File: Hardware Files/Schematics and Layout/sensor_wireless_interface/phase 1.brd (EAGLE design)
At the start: 100 x 80 mm, 5 parts, among them U1 RHD2216

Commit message: updated pin assignment for better routing
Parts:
- turned JP1 to 270 degrees
- turned JP2 to 0 degrees
- flipped JP3 to the top
- turned JP4 to 0 degrees
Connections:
- removed net N$12 (its old number): JP1.10, U1.12
- removed net N$2 (its old number): JP1.3, U1.2
- removed net N$56 (its old number): JP3.2, U1.36
- new net N$1: JP1.12, U1.12
- new net N$14: JP1.13, U1.13
- new net N$50: JP3.2, U1.30
- net N$10: now also JP1.8, U1.8; no longer JP1.6, U1.10
- net N$11: now also JP1.10, U1.10; no longer JP1.8, U1.11
- net N$13: now also JP1.11, U1.11; no longer JP1.12, U1.13
- net N$15: now also U1.56; no longer U1.43
- net N$16: now also U1.54; no longer U1.44
- net N$17: now also U1.52; no longer U1.45
- net N$19: now also U1.50; no longer U1.46
- net N$20: now also U1.48; no longer U1.47
- net N$21: now also U1.46; no longer U1.48
- net N$22: now also U1.44; no longer U1.49
- net N$23: now also JP2.2, U1.55; no longer JP2.14, U1.56
- net N$24: now also JP2.4, U1.53; no longer JP2.12, U1.55
- net N$25: now also JP2.6, U1.51; no longer JP2.10, U1.54
- net N$26: now also U1.49; no longer U1.53
- net N$27: now also JP2.10, U1.47; no longer JP2.6, U1.52
- net N$28: now also JP2.12, U1.45; no longer JP2.4, U1.51
- net N$29: now also JP2.14, U1.43; no longer JP2.2, U1.50
- net N$3: now also JP1.2, U1.2; no longer JP1.5, U1.3
- net N$30: now also JP4.2; no longer JP4.3
- net N$31: now also JP4.3; no longer JP4.5
- net N$32: now also JP4.4; no longer JP4.7
- net N$33: now also JP4.5; no longer JP4.9
- net N$34: now also JP4.6; no longer JP4.11
- net N$35: now also JP4.7; no longer JP4.13
- net N$36: now also JP4.8; no longer JP4.14
- net N$37: now also JP4.9; no longer JP4.12
- net N$39: now also JP4.11; no longer JP4.8
- net N$4: now also JP1.3, U1.3; no longer JP1.7, U1.4
- net N$40: now also JP4.12; no longer JP4.6
- net N$41: now also JP4.13; no longer JP4.4
- net N$42: now also JP4.14; no longer JP4.2
- net N$44: now also U1.31; no longer U1.30
- net N$45: now also U1.33; no longer U1.31
- net N$46: now also U1.35; no longer U1.32
- net N$47: now also U1.37; no longer U1.33
- net N$48: now also U1.39; no longer U1.34
- net N$49: now also U1.41; no longer U1.35
- net N$5: now also JP1.5; no longer JP1.9
- net N$51: now also JP3.4, U1.32; no longer JP3.12, U1.41
- net N$52: now also JP3.6, U1.34; no longer JP3.10, U1.40
- net N$53: now also U1.36; no longer U1.39
- net N$54: now also JP3.10; no longer JP3.6
- net N$55: now also JP3.12, U1.40; no longer JP3.4, U1.37
- net N$6: now also JP1.7, U1.7; no longer JP1.11, U1.6
- net N$7: now also JP1.9, U1.9; no longer JP1.13, U1.7
- net N$8: now also JP1.4, U1.4; no longer JP1.2, U1.8
- net N$9: now also JP1.6, U1.6; no longer JP1.4, U1.9

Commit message: changed to more specific schematic
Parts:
- removed JP4: (no value), pinhead:2X07
- added C1: 100nF, capacitor-wima:C2.5-2
- added C2: 10nF, capacitor-wima:C2.5-2
- JP1: device pinhead:2X07 -> pinhead:1X02
- JP2: device pinhead:2X07 -> pinhead:2X16
- JP3: device pinhead:2X07 -> pinhead:1X04
- moved JP3 32.4 mm to (52.1, 17.8), turned to 0 degrees
- moved JP1 7.73 mm to (29.2, 47.0)
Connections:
- removed net N$11: JP1.10, U1.10
- removed net N$12: JP1.14, U1.14
- removed net N$13: JP1.11, U1.11
- removed net N$14: JP1.13, U1.13
- removed net N$15: JP2.1, U1.56
- removed net N$16: JP2.3, U1.54
- removed net N$17: JP2.5, U1.52
- removed net N$18: JP4.1, U1.15
- removed net N$19: JP2.7, U1.50
- removed net N$2: JP1.1, U1.1
- removed net N$20: JP2.9, U1.48
- removed net N$21: JP2.11, U1.46
- removed net N$22: JP2.13, U1.44
- removed net N$23: JP2.2, U1.55
- removed net N$24: JP2.4, U1.53
- removed net N$25: JP2.6, U1.51
- removed net N$26: JP2.8, U1.49
- removed net N$27: JP2.10, U1.47
- removed net N$28: JP2.12, U1.45
- removed net N$29: JP2.14, U1.43
- removed net N$3: JP1.2, U1.2
- removed net N$30: JP4.2, U1.16
- removed net N$31: JP4.3, U1.17
- removed net N$32: JP4.4, U1.18
- removed net N$33: JP4.5, U1.19
- removed net N$34: JP4.6, U1.20
- removed net N$35: JP4.7, U1.21
- removed net N$36: JP4.8, U1.22
- removed net N$37: JP4.9, U1.23
- removed net N$38: JP4.10, U1.24
- removed net N$39: JP4.11, U1.25
- removed net N$4: JP1.3, U1.3
- removed net N$40: JP4.12, U1.26
- removed net N$41: JP4.13, U1.27
- removed net N$42: JP4.14, U1.28
- removed net N$43: JP3.1, U1.29
- removed net N$44: JP3.3, U1.31
- removed net N$45: JP3.5, U1.33
- removed net N$46: JP3.7, U1.35
- removed net N$47: JP3.9, U1.37
- removed net N$48: JP3.11, U1.39
- removed net N$49: JP3.13, U1.41
- removed net N$5: JP1.5, U1.5
- removed net N$50: JP3.2, U1.30
- removed net N$51: JP3.4, U1.32
- removed net N$52: JP3.6, U1.34
- removed net N$53: JP3.8, U1.36
- removed net N$54: JP3.10, U1.38
- removed net N$55: JP3.12, U1.40
- removed net N$56: JP3.14, U1.42
- removed net N$6: JP1.7, U1.7
- removed net N$7: JP1.9, U1.9
- removed net N$8: JP1.4, U1.4
- removed net N$9: JP1.6, U1.6
- new net AUXIN2: U1.15
- new net AUXIN3: U1.16
- new net AUX_OUT: U1.27
- new net CS_N: U1.18
- new net CS_P: JP3.1, U1.19
- new net GND: C1.2, C2.2, JP1.2, U1.11, U1.12, U1.17, U1.29, U1.30, U1.32
- new net IN0_N: JP2.2, U1.8
- new net IN0_P: JP2.1, U1.9
- new net IN10_N: JP2.22, U1.44
- new net IN10_P: JP2.21, U1.45
- new net IN11_N: JP2.24, U1.42
- new net IN11_P: JP2.23, U1.43
- new net IN12_N: JP2.26, U1.40
- new net IN12_P: JP2.25, U1.41
- new net IN13_N: JP2.28, U1.38
- new net IN13_P: JP2.27, U1.39
- new net IN14_N: JP2.30, U1.36
- new net IN14_P: JP2.29, U1.37
- new net IN15_N: JP2.32, U1.34
- new net IN15_P: JP2.31, U1.35
- new net IN1_N: JP2.4, U1.6
- new net IN1_P: JP2.3, U1.7
- new net IN2_N: JP2.6, U1.4
- new net IN2_P: JP2.5, U1.5
- new net IN3_N: JP2.8, U1.2
- new net IN3_P: JP2.7, U1.3
- new net IN4_N: JP2.10, U1.56
- new net IN4_P: JP2.9, U1.1
- new net IN5_N: JP2.12, U1.54
- new net IN5_P: JP2.11, U1.55
- new net IN6_N: JP2.14, U1.52
- new net IN6_P: JP2.13, U1.53
- new net IN7_N: JP2.16, U1.50
- new net IN7_P: JP2.15, U1.51
- new net IN8_N: JP2.18, U1.48
- new net IN8_P: JP2.17, U1.49
- new net IN9_N: JP2.20, U1.46
- new net IN9_P: JP2.19, U1.47
- new net MISO_N: U1.24
- new net MISO_P: JP3.4, U1.25
- new net MOSI_N: U1.22
- new net MOSI_P: JP3.3, U1.23
- new net SCLK_N: U1.20
- new net SCLK_P: JP3.2, U1.21
- new net VDD: C1.1, JP1.1, U1.13, U1.26, U1.31
- net N$1: now also C2.1, U1.28; no longer JP1.12, U1.12
- net N$10: now also U1.33; no longer JP1.8, U1.8

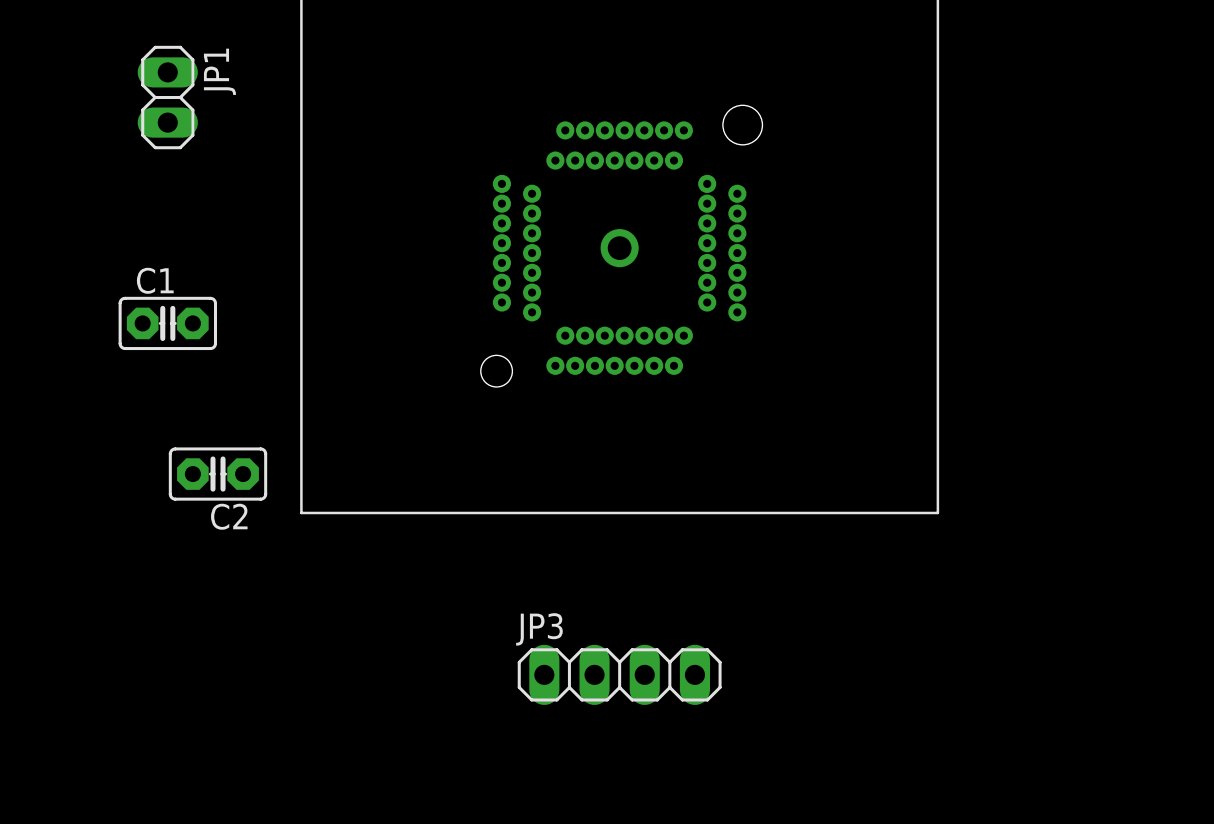
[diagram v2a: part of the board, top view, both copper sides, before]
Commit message: added another pin header for AUXIN*
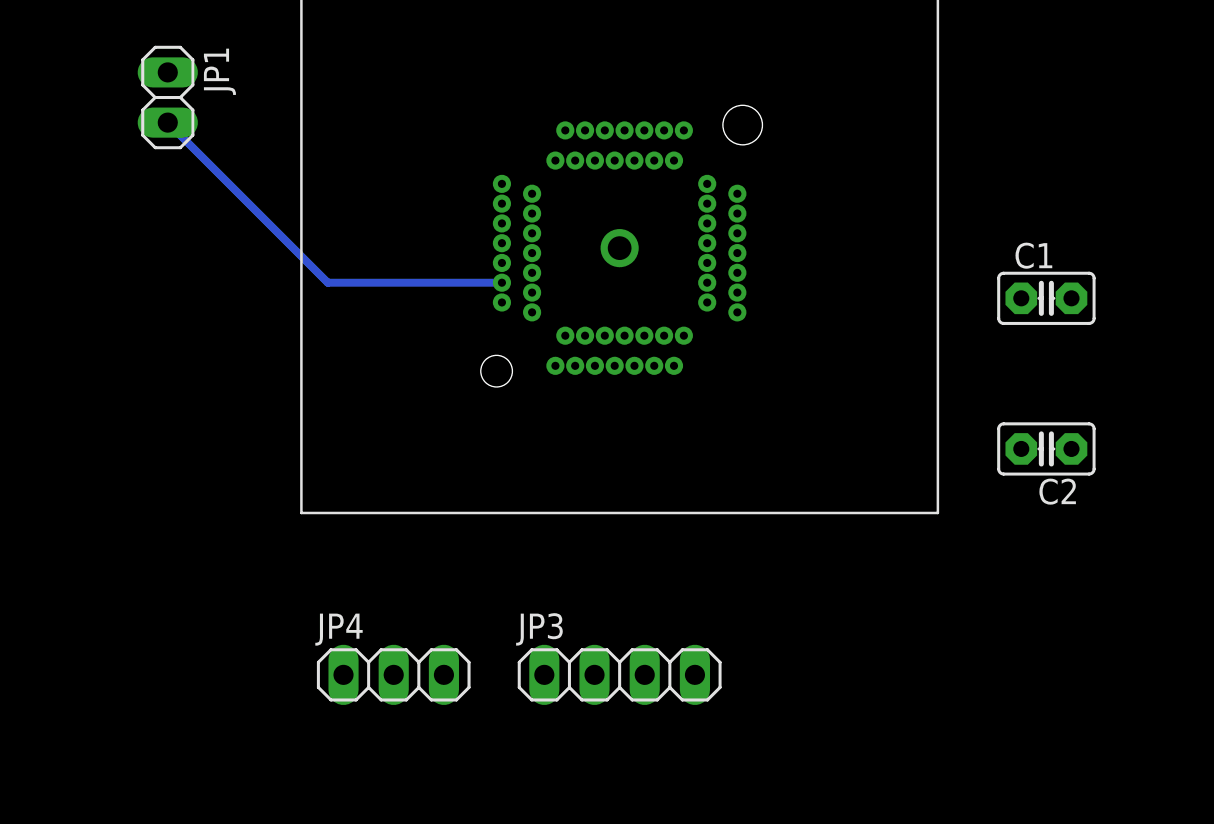
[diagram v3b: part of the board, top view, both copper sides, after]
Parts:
- added JP4: (no value), pinhead:1X03
- moved C1 44.5 mm to (73.7, 36.8)
- moved C2 41.9 mm to (73.7, 29.2)
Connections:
- removed net CS_N: U1.18
- removed net MISO_N: U1.24
- removed net MOSI_N: U1.22
- removed net N$10: U1.33
- removed net SCLK_N: U1.20
- new net AUXIN1: JP4.1, U1.14
- net AUXIN2: now also JP4.2
- net AUXIN3: now also JP4.3
- net GND: now also U1.10
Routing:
- net GND: track 0.00 -> 20.3 mm
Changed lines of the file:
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@@
 <element name="JP2" library="pinhead" package="2X16" value="" x="52.07" y="59.69"/>
 <element name="JP3" library="pinhead" package="1X04" value="" x="52.07" y="17.78"/>
-<element name="C1" library="capacitor-wima" package="C2.5-2" value="100nF" x="29.21" y="35.56"/>
-<element name="C2" library="capacitor-wima" package="C2.5-2" value="10nF" x="31.75" y="27.94" rot="R180"/>
+<element name="C1" library="capacitor-wima" package="C2.5-2" value="100nF" x="73.66" y="36.83"/>
+<element name="C2" library="capacitor-wima" package="C2.5-2" value="10nF" x="73.66" y="29.21" rot="R180"/>
+<element name="JP4" library="pinhead" package="1X03" value="" x="40.64" y="17.78"/>
 </elements>
 <signals>
@@
 <wire x1="46.115" y1="36.62" x2="54.32" y2="34.94" width="0" layer="19" extent="1-1"/>
 <wire x1="29.21" y1="48.26" x2="46.115" y2="36.62" width="0" layer="19" extent="1-1"/>
-<wire x1="27.94" y1="35.56" x2="29.21" y2="48.26" width="0" layer="19" extent="1-1"/>
+<wire x1="72.39" y1="36.83" x2="29.21" y2="48.26" width="0" layer="19" extent="1-1"/>
 </signal>
 <signal name="GND">
@@
 <contactref element="C2" pad="2"/>
 <contactref element="U1" pad="32"/>
+<contactref element="U1" pad="10"/>
+<wire x1="46.115" y1="37.62" x2="37.31" y2="37.62" width="0.4064" layer="16"/>
+<wire x1="37.31" y1="37.62" x2="29.21" y2="45.72" width="0.4064" layer="16"/>
 <wire x1="56.5" y1="37.62" x2="56.5" y2="36.62" width="0" layer="19" extent="1-1"/>
 <wire x1="58.025" y1="36.12" x2="56.5" y2="36.62" width="0" layer="19" extent="1-1"/>
 <wire x1="49.82" y1="33.415" x2="56.5" y2="36.62" width="0" layer="19" extent="1-1"/>
 <wire x1="47.64" y1="37.12" x2="49.82" y2="33.415" width="0" layer="19" extent="1-1"/>
+<wire x1="47.64" y1="38.12" x2="47.64" y2="37.12" width="0" layer="19" extent="1-1"/>
 <wire x1="46.115" y1="37.62" x2="47.64" y2="37.12" width="0" layer="19" extent="1-1"/>
-<wire x1="29.21" y1="45.72" x2="46.115" y2="37.62" width="0" layer="19" extent="1-1"/>
-<wire x1="30.48" y1="35.56" x2="29.21" y2="45.72" width="0" layer="19" extent="1-1"/>
-<wire x1="30.48" y1="27.94" x2="30.48" y2="35.56" width="0" layer="19" extent="1-1"/>
+<wire x1="74.93" y1="36.83" x2="37.31" y2="37.62" width="0" layer="19" extent="16-16"/>
+<wire x1="72.39" y1="29.21" x2="74.93" y2="36.83" width="0" layer="19" extent="1-1"/>
 </signal>
 <signal name="AUXIN2">
 <contactref element="U1" pad="15"/>
+<contactref element="JP4" pad="2"/>
+<wire x1="40.64" y1="17.78" x2="48.82" y2="33.415" width="0" layer="19" extent="1-1"/>
 </signal>
 <signal name="AUXIN3">
 <contactref element="U1" pad="16"/>
-</signal>
-<signal name="CS_N">
-<contactref element="U1" pad="18"/>
+<contactref element="JP4" pad="3"/>
+<wire x1="43.18" y1="17.78" x2="49.32" y2="34.94" width="0" layer="19" extent="1-1"/>
 </signal>
 <signal name="CS_P">
@@
 <wire x1="48.26" y1="17.78" x2="50.82" y2="33.415" width="0" layer="19" extent="1-1"/>
 </signal>
-<signal name="SCLK_N">
-<contactref element="U1" pad="20"/>
-</signal>
 <signal name="SCLK_P">
 <contactref element="U1" pad="21"/>
@@
 <wire x1="50.8" y1="17.78" x2="51.82" y2="33.415" width="0" layer="19" extent="1-1"/>
 </signal>
-<signal name="MOSI_N">
-<contactref element="U1" pad="22"/>
-</signal>
 <signal name="MOSI_P">
 <contactref element="U1" pad="23"/>
@@
 <wire x1="53.34" y1="17.78" x2="52.82" y2="33.415" width="0" layer="19" extent="1-1"/>
 </signal>
-<signal name="MISO_N">
-<contactref element="U1" pad="24"/>
-</signal>
 <signal name="MISO_P">
 <contactref element="U1" pad="25"/>
@@
 <wire x1="71.12" y1="60.96" x2="56.5" y2="38.62" width="0" layer="19" extent="1-1"/>
 </signal>
-<signal name="N$10">
-<contactref element="U1" pad="33"/>
-</signal>
 <signal name="IN12_P">
 <contactref element="JP2" pad="25"/>
@@
 <contactref element="U1" pad="28"/>
 <contactref element="C2" pad="1"/>
-<wire x1="33.02" y1="27.94" x2="55.32" y2="34.94" width="0" layer="19" extent="1-1"/>
+<wire x1="74.93" y1="29.21" x2="55.32" y2="34.94" width="0" layer="19" extent="1-1"/>
+</signal>
+<signal name="AUXIN1">
+<contactref element="JP4" pad="1"/>
+<contactref element="U1" pad="14"/>
+<wire x1="38.1" y1="17.78" x2="47.64" y2="36.12" width="0" layer="19" extent="1-1"/>
 </signal>
 </signals>

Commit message: connect AUXIN1-2-3 to VDD to save power
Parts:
- removed JP4: (no value), pinhead:1X03
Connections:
- removed net AUXIN1: JP4.1, U1.14
- removed net AUXIN2: JP4.2, U1.15
- removed net AUXIN3: JP4.3, U1.16
- net VDD: now also U1.14, U1.15, U1.16
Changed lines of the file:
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@@
 <element name="C1" library="capacitor-wima" package="C2.5-2" value="100nF" x="73.66" y="36.83"/>
 <element name="C2" library="capacitor-wima" package="C2.5-2" value="10nF" x="73.66" y="29.21" rot="R180"/>
-<element name="JP4" library="pinhead" package="1X03" value="" x="40.64" y="17.78"/>
 </elements>
 <signals>
@@
 <contactref element="C1" pad="1"/>
 <contactref element="U1" pad="31"/>
+<contactref element="U1" pad="14"/>
+<contactref element="U1" pad="15"/>
+<contactref element="U1" pad="16"/>
+<wire x1="58.025" y1="37.12" x2="72.39" y2="36.83" width="0" layer="19" extent="1-1"/>
 <wire x1="54.32" y1="34.94" x2="58.025" y2="37.12" width="0" layer="19" extent="1-1"/>
-<wire x1="46.115" y1="36.62" x2="54.32" y2="34.94" width="0" layer="19" extent="1-1"/>
+<wire x1="49.32" y1="34.94" x2="54.32" y2="34.94" width="0" layer="19" extent="1-1"/>
+<wire x1="48.82" y1="33.415" x2="49.32" y2="34.94" width="0" layer="19" extent="1-1"/>
+<wire x1="47.64" y1="36.12" x2="49.32" y2="34.94" width="0" layer="19" extent="1-1"/>
+<wire x1="46.115" y1="36.62" x2="47.64" y2="36.12" width="0" layer="19" extent="1-1"/>
 <wire x1="29.21" y1="48.26" x2="46.115" y2="36.62" width="0" layer="19" extent="1-1"/>
-<wire x1="72.39" y1="36.83" x2="29.21" y2="48.26" width="0" layer="19" extent="1-1"/>
 </signal>
 <signal name="GND">
@@
 <wire x1="72.39" y1="29.21" x2="74.93" y2="36.83" width="0" layer="19" extent="1-1"/>
 </signal>
-<signal name="AUXIN2">
-<contactref element="U1" pad="15"/>
-<contactref element="JP4" pad="2"/>
-<wire x1="40.64" y1="17.78" x2="48.82" y2="33.415" width="0" layer="19" extent="1-1"/>
-</signal>
-<signal name="AUXIN3">
-<contactref element="U1" pad="16"/>
-<contactref element="JP4" pad="3"/>
-<wire x1="43.18" y1="17.78" x2="49.32" y2="34.94" width="0" layer="19" extent="1-1"/>
-</signal>
 <signal name="CS_P">
 <contactref element="U1" pad="19"/>
@@
 <wire x1="74.93" y1="29.21" x2="55.32" y2="34.94" width="0" layer="19" extent="1-1"/>
 </signal>
-<signal name="AUXIN1">
-<contactref element="JP4" pad="1"/>
-<contactref element="U1" pad="14"/>
-<wire x1="38.1" y1="17.78" x2="47.64" y2="36.12" width="0" layer="19" extent="1-1"/>
-</signal>
 </signals>
